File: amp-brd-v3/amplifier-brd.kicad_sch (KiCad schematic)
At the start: 12 parts, among them J1 VOUT, J2 VOUT, Q1 BSS84, U3 DS28EA00

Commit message: Modified DAC, AMP v2 and Mezzanine to support AMP v3. Finished AMP v3 design.
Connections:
- net EN: now also BOT1.38 (Pin_38), TOP1.38 (Pin_38)
- net GND: no longer BOT1.38 (Pin_38), TOP1.38 (Pin_38)
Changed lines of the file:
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@@
-	)
-	(junction
-		(at 250.19 83.82)
-		(diameter 0)
-		(color 0 0 0 0)
 	)
 	(junction
@@
 	(junction
 		(at 154.94 106.68)
-		(diameter 0)
-		(color 0 0 0 0)
-	)
-	(junction
-		(at 190.5 83.82)
 		(diameter 0)
 		(color 0 0 0 0)
@@
 	(wire
 		(pts
-			(xy 177.8 83.82) (xy 190.5 83.82)
-		)
-		(stroke
-			(width 0)
-			(type default)
-		)
-	)
-	(wire
-		(pts
 			(xy 154.94 121.92) (xy 165.1 121.92)
 		)
@@
 	(wire
 		(pts
-			(xy 190.5 83.82) (xy 190.5 99.06)
+			(xy 190.5 81.28) (xy 190.5 99.06)
 		)
 		(stroke
@@
 	(wire
 		(pts
-			(xy 250.19 81.28) (xy 250.19 83.82)
+			(xy 250.19 81.28) (xy 250.19 99.06)
 		)
 		(stroke
@@
 	(wire
 		(pts
+			(xy 177.8 83.82) (xy 186.69 83.82)
+		)
+		(stroke
+			(width 0)
+			(type default)
+		)
+	)
+	(wire
+		(pts
 			(xy 45.72 90.17) (xy 55.88 90.17)
 		)
@@
 	(wire
 		(pts
-			(xy 250.19 83.82) (xy 250.19 99.06)
-		)
-		(stroke
-			(width 0)
-			(type default)
-		)
-	)
-	(wire
-		(pts
 			(xy 214.63 111.76) (xy 224.79 111.76)
 		)
@@
 	(wire
 		(pts
-			(xy 190.5 81.28) (xy 190.5 83.82)
-		)
-		(stroke
-			(width 0)
-			(type default)
-		)
-	)
-	(wire
-		(pts
 			(xy 171.45 135.89) (xy 171.45 139.7)
 		)
@@
 	(wire
 		(pts
+			(xy 237.49 83.82) (xy 246.38 83.82)
+		)
+		(stroke
+			(width 0)
+			(type default)
+		)
+	)
+	(wire
+		(pts
 			(xy 214.63 104.14) (xy 214.63 106.68)
 		)
@@
 		(pts
 			(xy 177.8 114.3) (xy 186.69 114.3)
-		)
-		(stroke
-			(width 0)
-			(type default)
-		)
-	)
-	(wire
-		(pts
-			(xy 237.49 83.82) (xy 250.19 83.82)
 		)
 		(stroke
@@
 		)
 	)
+	(label "EN"
+		(at 246.38 83.82 180)
+		(effects
+			(font
+				(size 1.27 1.27)
+			)
+			(justify right bottom)
+		)
+	)
 	(label "A1"
 		(at 45.72 81.28 0)
@@
 		)
 	)
+	(label "EN"
+		(at 186.69 83.82 180)
+		(effects
+			(font
+				(size 1.27 1.27)
+			)
+			(justify right bottom)
+		)
+	)

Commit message: Optimized temperature sensor from Kuravi's design, reworked inductor placement in amp board v3
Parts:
- R7: value 10k -> 100k
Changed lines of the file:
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@@
 			)
 		)
-		(property "Value" "10k"
+		(property "Value" "100k"
 			(at 110.49 124.4599 0)
 			(effects

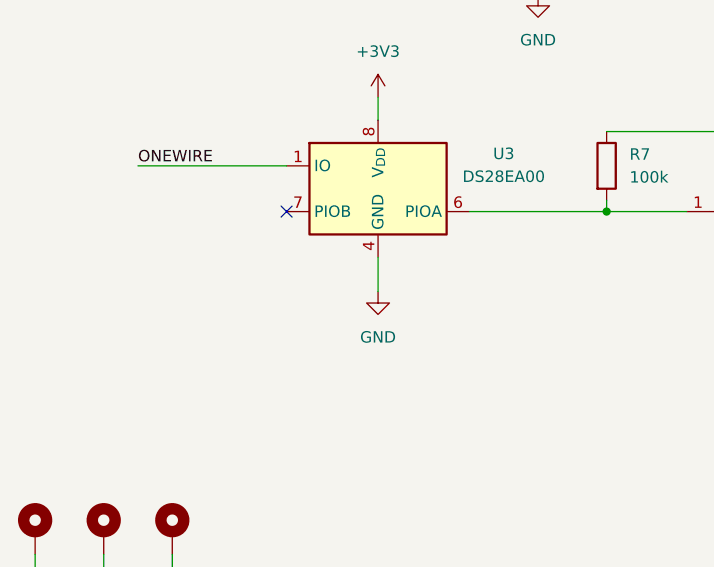
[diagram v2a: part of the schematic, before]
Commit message: Tested DAC and INA, doing new boards
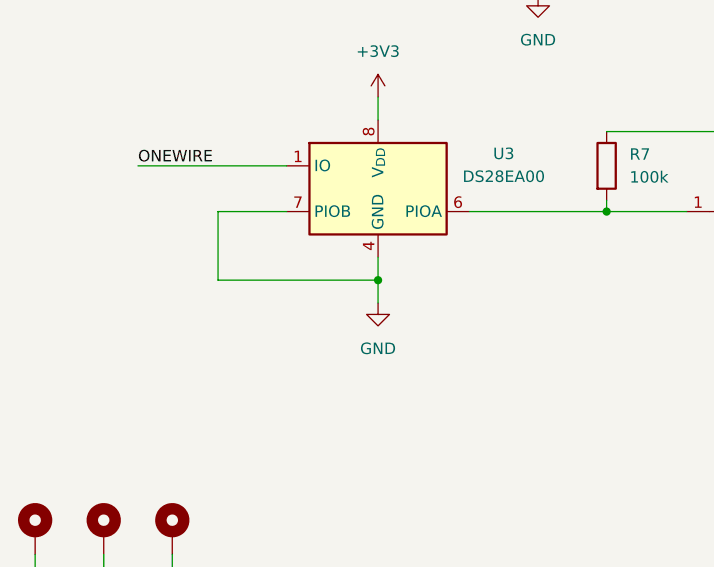
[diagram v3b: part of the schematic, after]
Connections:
- net GND: now also U3.7 (PIOB)
- no-connect marks 3 -> 2
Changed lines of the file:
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@@
+	)
+	(junction
+		(at 82.55 135.89)
+		(diameter 0)
+		(color 0 0 0 0)
 	)
 	(junction
@@
 	)
 	(no_connect
-		(at 72.39 128.27)
-	)
-	(no_connect
 		(at 186.69 96.52)
 	)
@@
 	(wire
 		(pts
+			(xy 82.55 135.89) (xy 82.55 138.43)
+		)
+		(stroke
+			(width 0)
+			(type default)
+		)
+	)
+	(wire
+		(pts
 			(xy 154.94 88.9) (xy 165.1 88.9)
 		)
@@
 	(wire
 		(pts
+			(xy 72.39 128.27) (xy 64.77 128.27)
+		)
+		(stroke
+			(width 0)
+			(type default)
+		)
+	)
+	(wire
+		(pts
 			(xy 59.69 168.91) (xy 59.69 166.37)
 		)
@@
 	(wire
 		(pts
-			(xy 82.55 133.35) (xy 82.55 137.16)
+			(xy 82.55 133.35) (xy 82.55 135.89)
 		)
 		(stroke
@@
 	(wire
 		(pts
+			(xy 64.77 128.27) (xy 64.77 135.89)
+		)
+		(stroke
+			(width 0)
+			(type default)
+		)
+	)
+	(wire
+		(pts
 			(xy 44.45 166.37) (xy 44.45 168.91)
 		)
@@
 		(pts
 			(xy 214.63 91.44) (xy 224.79 91.44)
+		)
+		(stroke
+			(width 0)
+			(type default)
+		)
+	)
+	(wire
+		(pts
+			(xy 64.77 135.89) (xy 82.55 135.89)
 		)
 		(stroke
@@
 	(symbol
 		(lib_id "power:GND")
-		(at 82.55 137.16 0)
+		(at 82.55 138.43 0)
 		(unit 1)
 		(exclude_from_sim no)
@@
 		(fields_autoplaced yes)
 		(property "Reference" "#PWR021"
+			(at 82.55 144.78 0)
+			(effects
+				(font
+					(size 1.27 1.27)
+				)
+				(hide yes)
+			)
+		)
+		(property "Value" "GND"
 			(at 82.55 143.51 0)
 			(effects
@@
 					(size 1.27 1.27)
 				)
-				(hide yes)
-			)
-		)
-		(property "Value" "GND"
-			(at 82.55 142.24 0)
-			(effects
-				(font
-					(size 1.27 1.27)
-				)
 			)
 		)
 		(property "Footprint" ""
-			(at 82.55 137.16 0)
+			(at 82.55 138.43 0)
 			(effects
 				(font
@@
 		)
 		(property "Datasheet" ""
-			(at 82.55 137.16 0)
+			(at 82.55 138.43 0)
 			(effects
 				(font
@@
 		)
 		(property "Description" "Power symbol creates a global label with name \"GND\" , ground"
-			(at 82.55 137.16 0)
-			(effects
-				(font
+			(at 82.55 138.43 0)
+			(effects
+				(font

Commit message: Updated all boards for production
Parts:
- removed J2: VOUT, Connector_PinHeader_2.54mm:PinHeader_1x02_P2.54mm_Vertical, symbol Connector_Generic:Conn_01x02
- J1: footprint Connector_Molex:Molex_PicoBlade_53261-0471_1x04-1MP_P1.25mm_Horizontal -> Connector_Molex:Molex_PicoBlade_53261-0271_1x02-1MP_P1.25mm_Horizontal; symbol Connector_Generic_MountingPin:Conn_01x04_MountingPin -> Connector_Generic_MountingPin:Conn_01x02_MountingPin; Mfr # 53261-0471 -> 53261-0271; Mouser https://www.mouser.com/ProductDetail/Molex/53261-0471?qs=%2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 -> https://www.mouser.com/ProductDetail/Molex/53261-0271?qs=%2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; Mouser # 538-53261-0471 -> 538-53261-0271
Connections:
- net GND: now also J1.2 (Pin_2); no longer J1.3 (Pin_3), J1.4 (Pin_4)
- net OP AMP/V_{OUT}: no longer J1.2 (Pin_2)
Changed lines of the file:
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@@
-	)
-	(junction
-		(at 110.49 96.52)
-		(diameter 0)
-		(color 0 0 0 0)
 	)
 	(junction
@@
 	)
 	(junction
-		(at 102.87 81.28)
-		(diameter 0)
-		(color 0 0 0 0)
-	)
-	(junction
 		(at 214.63 106.68)
 		(diameter 0)
@@
 	)
 	(junction
-		(at 102.87 86.36)
-		(diameter 0)
-		(color 0 0 0 0)
-	)
-	(junction
 		(at 214.63 116.84)
 		(diameter 0)
@@
 	(junction
 		(at 154.94 106.68)
-		(diameter 0)
-		(color 0 0 0 0)
-	)
-	(junction
-		(at 102.87 83.82)
 		(diameter 0)
 		(color 0 0 0 0)
@@
 	(wire
 		(pts
-			(xy 86.36 83.82) (xy 102.87 83.82)
+			(xy 86.36 83.82) (xy 105.41 83.82)
 		)
 		(stroke
@@
 	(wire
 		(pts
-			(xy 119.38 78.74) (xy 102.87 78.74)
-		)
-		(stroke
-			(width 0)
-			(type default)
-		)
-	)
-	(wire
-		(pts
 			(xy 154.94 99.06) (xy 165.1 99.06)
 		)
@@
 	(wire
 		(pts
-			(xy 102.87 88.9) (xy 102.87 86.36)
-		)
-		(stroke
-			(width 0)
-			(type default)
-		)
-	)
-	(wire
-		(pts
 			(xy 151.13 124.46) (xy 151.13 127)
 		)
@@
 	(wire
 		(pts
-			(xy 105.41 81.28) (xy 102.87 81.28)
-		)
-		(stroke
-			(width 0)
-			(type default)
-		)
-	)
-	(wire
-		(pts
 			(xy 231.14 135.89) (xy 231.14 139.7)
 		)
@@
 	(wire
 		(pts
-			(xy 102.87 86.36) (xy 100.33 86.36)
-		)
-		(stroke
-			(width 0)
-			(type default)
-		)
-	)
-	(wire
-		(pts
-			(xy 119.38 86.36) (xy 119.38 96.52)
+			(xy 100.33 86.36) (xy 105.41 86.36)
 		)
 		(stroke
@@
 	(wire
 		(pts
-			(xy 110.49 93.98) (xy 110.49 96.52)
-		)
-		(stroke
-			(width 0)
-			(type default)
-		)
-	)
-	(wire
-		(pts
-			(xy 121.92 86.36) (xy 119.38 86.36)
-		)
-		(stroke
-			(width 0)
-			(type default)
-		)
-	)
-	(wire
-		(pts
 			(xy 214.63 99.06) (xy 214.63 101.6)
 		)
@@
 	(wire
 		(pts
-			(xy 110.49 96.52) (xy 119.38 96.52)
-		)
-		(stroke
-			(width 0)
-			(type default)
-		)
-	)
-	(wire
-		(pts
 			(xy 237.49 93.98) (xy 246.38 93.98)
 		)
@@
 	(wire
 		(pts
-			(xy 121.92 83.82) (xy 119.38 83.82)
-		)
-		(stroke
-			(width 0)
-			(type default)
-		)
-	)
-	(wire
-		(pts
 			(xy 55.88 123.19) (xy 72.39 123.19)
 		)
@@
 	(wire
 		(pts
-			(xy 102.87 81.28) (xy 102.87 83.82)
-		)
-		(stroke
-			(width 0)
-			(type default)
-		)
-	)
-	(wire
-		(pts
 			(xy 250.19 135.89) (xy 231.14 135.89)
 		)
@@
 	(wire
 		(pts
-			(xy 119.38 83.82) (xy 119.38 78.74)
-		)
-		(stroke
-			(width 0)
-			(type default)
-		)
-	)
-	(wire
-		(pts
 			(xy 237.49 78.74) (xy 250.19 78.74)
 		)
@@
 	(wire
 		(pts
-			(xy 105.41 88.9) (xy 102.87 88.9)
-		)
-		(stroke
-			(width 0)
-			(type default)
-		)
-	)
-	(wire
-		(pts
 			(xy 100.33 86.36) (xy 100.33 96.52)
 		)
@@
 	(wire
 		(pts
-			(xy 102.87 78.74) (xy 102.87 81.28)
+			(xy 110.49 91.44) (xy 110.49 96.52)
 		)
 		(stroke
@@
 		(pts
 			(xy 52.07 166.37) (xy 52.07 168.91)
-		)
-		(stroke
-			(width 0)
-			(type default)
-		)
-	)
-	(wire
-		(pts
-			(xy 102.87 83.82) (xy 105.41 83.82)
-		)
-		(stroke
-			(width 0)
-			(type default)
-		)
-	)
-	(wire
-		(pts
-			(xy 105.41 86.36) (xy 102.87 86.36)
 		)
 		(stroke
@@
 			)
 			(justify right bottom)
-		)
-	)
-	(symbol
-		(lib_id "Connector_Generic:Conn_01x02")
-		(at 127 83.82 0)
-		(unit 1)
-		(exclude_from_sim no)
-		(in_bom yes)
-		(on_board yes)
-		(dnp yes)
-		(fields_autoplaced yes)
-		(property "Reference" "J2"
-			(at 129.54 83.8199 0)
-			(effects
-				(font
-					(size 1.27 1.27)
-				)
-				(justify left)
-			)
-		)
-		(property "Value" "VOUT"
-			(at 129.54 86.3599 0)
-			(effects
-				(font
-					(size 1.27 1.27)
-				)
-				(justify left)
-			)
-		)
-		(property "Footprint" "Connector_PinHeader_2.54mm:PinHeader_1x02_P2.54mm_Vertical"
-			(at 127 83.82 0)
-			(effects
-				(font
-					(size 1.27 1.27)
-				)
-				(hide yes)
-			)
-		)
-		(property "Datasheet" "~"
-			(at 127 83.82 0)
-			(effects
-				(font
-					(size 1.27 1.27)
-				)
-				(hide yes)
-			)
-		)
-		(property "Description" "Generic connector, single row, 01x02, script generated (kicad-library-utils/schlib/autogen/connector/)"
-			(at 127 83.82 0)
-			(effects
-				(font
-					(size 1.27 1.27)
-				)
-				(hide yes)
-			)
-		)
-		(pin "2"
-		)
-		(pin "1"
-		)
-		(instances
-			(project ""
-				(path "/4a199ccc-be1f-4132-9551-a46e36599bcb"
-					(reference "J2")
-					(unit 1)
-				)
-			)
 		)
 	)
@@
 	)
 	(symbol
-		(lib_id "Connector_Generic_MountingPin:Conn_01x04_MountingPin")
+		(lib_id "Connector_Generic_MountingPin:Conn_01x02_MountingPin")
 		(at 110.49 83.82 0)
 		(unit 1)
@@
 			)
 		)
-		(property "Footprint" "Connector_Molex:Molex_PicoBlade_53261-0471_1x04-1MP_P1.25mm_Horizontal"
+		(property "Footprint" "Connector_Molex:Molex_PicoBlade_53261-0271_1x02-1MP_P1.25mm_Horizontal"
 			(at 110.49 83.82 0)
 			(effects
@@
 			)
 		)
-		(property "Datasheet" "https://www.molex.com/en-us/products/part-detail-pdf/532610471?display=pdf"
+		(property "Datasheet" "~"
 			(at 110.49 83.82 0)
 			(effects
@@
 			)
 		)
-		(property "Description" "Headers & Wire Housings PicoBlade1.25 SMT RA PKG 4P"
+		(property "Description" "Headers & Wire Housings PicoBlade1.25 SMT RA PKG 2P"
 			(at 110.49 83.82 0)
 			(effects
@@
 			)
 		)
-		(property "Mfr #" "53261-0471"
+		(property "Mfr #" "53261-0271"
 			(at 110.49 83.82 0)
 			(effects
@@
 			)
 		)
-		(property "Mouser #" "538-53261-0471"
+		(property "Mouser #" "538-53261-0271"
 			(at 110.49 83.82 0)
 			(effects
@@
 			)
 		)
-		(property "Mouser" "https://www.mouser.com/ProductDetail/Molex/53261-0471?qs=%252B72YyncTwW9e3et3PwnEMw%3D%3D&utm_id=22310811105&utm_source=google&utm_medium=cpc&utm_marketing_tactic=amermsp&gad_source=1&gad_campaignid=22310815365&gbraid=0AAAAADn_wf1zNbovdi8o5BkocC-mYGcy3&gclid=Cj0KCQiAosrJBhD0ARIsAHebCNoqHSlv8093uII-LEywz99gd4VTBqkxKpseFi77wLe4p3ZZiX-RvZsaAr9zEALw_wcB"
+		(property "Mouser" "https://www.mouser.com/ProductDetail/Molex/53261-0271?qs=%252B72YyncTwW%252B8%252BBjraxGf3A%3D%3D"
 			(at 110.49 83.82 0)
 			(effects
@@
 		(pin "1"
 		)
-		(pin "3"
-		)
-		(pin "4"
-		)
 		(pin "2"

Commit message: Added part numbers
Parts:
- BOT1: Mfr (none) -> Amphenol FCI; Mfr # (none) -> 10132798-042100LF; Package (none) -> SMD
- D1: Mfr (none) -> Dialight; Mfr # (none) -> 598-2A00-107F; Package (none) -> 0402
- J1: Package (none) -> SMD
- Q1: Mfr (none) -> onsemi; Mfr # (none) -> BSS84; Package (none) -> SOT-23
- R6: Mfr (none) -> TE Connectivity / Holsworthy; Mfr # (none) -> RP73PF1E1K0BTD; Package (none) -> 0402
- R7: Mfr (none) -> Vishay-Dale; Mfr # (none) -> CRCW0402100KFKED; Package (none) -> 0402
- TOP1: Mfr (none) -> Amphenol ICC (FCI); Mfr # (none) -> 10132797-045100LF; Package (none) -> SMD
- U3: Mfr (none) -> Analog Devices Inc./Maxim Integrated; Mfr # (none) -> DS28EA00U+; Package (none) -> SMD
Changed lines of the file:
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@@
+			)
+		)
+		(property "Package" "SMD"
+			(at 110.49 83.82 0)
+			(effects
+				(font
+					(size 1.27 1.27)
+				)
+				(hide yes)
 			)
 		)
@@
 			)
 		)
-		(property "Description" "Generic connectable mounting pin connector, double row, 02x20, counter clockwise pin numbering scheme (similar to DIP package numbering), script generated (kicad-library-utils/schlib/autogen/connector/)"
+		(property "Description" "Board to Board & Mezzanine Connectors HEIGHT REC CONNECTOR"
+			(at 229.87 101.6 0)
+			(effects
+				(font
+					(size 1.27 1.27)
+				)
+				(hide yes)
+			)
+		)
+		(property "Package" "SMD"
+			(at 229.87 101.6 0)
+			(effects
+				(font
+					(size 1.27 1.27)
+				)
+				(hide yes)
+			)
+		)
+		(property "Mfr" "Amphenol FCI"
+			(at 229.87 101.6 0)
+			(effects
+				(font
+					(size 1.27 1.27)
+				)
+				(hide yes)
+			)
+		)
+		(property "Mfr #" "10132798-042100LF"
 			(at 229.87 101.6 0)
 			(effects
@@
 			)
 		)
-		(property "Description" "Light emitting diode"
+		(property "Description" "White LEDs 0402 SMD WHITE 5mA 2.4V 66mW"
 			(at 124.46 156.21 0)
 			(effects
@@
 			)
 		)
+		(property "Package" "0402"
+			(at 124.46 156.21 90)
+			(effects
+				(font
+					(size 1.27 1.27)
+				)
+				(hide yes)
+			)
+		)
+		(property "Mfr #" "598-2A00-107F "
+			(at 124.46 156.21 90)
+			(effects
+				(font
+					(size 1.27 1.27)
+				)
+				(hide yes)
+			)
+		)
+		(property "Mfr" "Dialight "
+			(at 124.46 156.21 90)
+			(effects
+				(font
+					(size 1.27 1.27)
+				)
+				(hide yes)
+			)
+		)
 		(pin "2"
 		)
@@
 			)
 		)
-		(property "Description" "1-Wire Digital Thermometer with Sequence Detect and PIO"
+		(property "Description" "Temperature Sensor Digital, Local -40°C ~ 85°C 11 b 8-uMAX/uSOP"
+			(at 82.55 125.73 0)
+			(effects
+				(font
+					(size 1.27 1.27)
+				)
+				(hide yes)
+			)
+		)
+		(property "Mfr" "Analog Devices Inc./Maxim Integrated"
+			(at 82.55 125.73 0)
+			(effects
+				(font
+					(size 1.27 1.27)
+				)
+				(hide yes)
+			)
+		)
+		(property "Mfr #" "DS28EA00U+"
+			(at 82.55 125.73 0)
+			(effects
+				(font
+					(size 1.27 1.27)
+				)
+				(hide yes)
+			)
+		)
+		(property "Package" "SMD"
 			(at 82.55 125.73 0)
 			(effects
@@
 			)
 		)
-		(property "Description" "Generic connectable mounting pin connector, double row, 02x20, counter clockwise pin numbering scheme (similar to DIP package numbering), script generated (kicad-library-utils/schlib/autogen/connector/)"
+		(property "Description" "40 Position Connector Plug, Outer Shroud Contacts Surface Mount Gold"
+			(at 170.18 101.6 0)
+			(effects
+				(font
+					(size 1.27 1.27)
+				)
+				(hide yes)
+			)
+		)
+		(property "Mfr" "Amphenol ICC (FCI)"
+			(at 170.18 101.6 0)
+			(effects
+				(font
+					(size 1.27 1.27)
+				)
+				(hide yes)
+			)
+		)
+		(property "Mfr #" "10132797-045100LF"
+			(at 170.18 101.6 0)
+			(effects
+				(font
+					(size 1.27 1.27)
+				)
+				(hide yes)
+			)
+		)
+		(property "Package" "SMD"
 			(at 170.18 101.6 0)
 			(effects
@@
 			)
 		)
-		(property "Description" "Resistor"
+		(property "Description" "Thin Film Resistors HP PrecisionResistor 1E 0.1W 1K0"
+			(at 124.46 143.51 0)
+			(effects
+				(font
+					(size 1.27 1.27)
+				)
+				(hide yes)
+			)
+		)
+		(property "Package" "0402"
+			(at 124.46 143.51 0)
+			(effects
+				(font
+					(size 1.27 1.27)
+				)
+				(hide yes)
+			)
+		)
+		(property "Mfr" "TE Connectivity / Holsworthy "
+			(at 124.46 143.51 0)
+			(effects
+				(font
+					(size 1.27 1.27)
+				)
+				(hide yes)
+			)
+		)
+		(property "Mfr #" "RP73PF1E1K0BTD "
 			(at 124.46 143.51 0)
 			(effects
@@
 			)
 		)
-		(property "Description" "Resistor"
+		(property "Description" "Thick Film Resistors - SMD 1/10 Watt 100Kohms 1%"
+			(at 107.95 123.19 0)
+			(effects
+				(font
+					(size 1.27 1.27)
+				)
+				(hide yes)
+			)
+		)
+		(property "Mfr" "Vishay-Dale"
+			(at 107.95 123.19 0)
+			(effects
+				(font
+					(size 1.27 1.27)
+				)
+				(hide yes)
+			)
+		)
+		(property "Mfr #" "CRCW0402100KFKED"
+			(at 107.95 123.19 0)
+			(effects
+				(font
+					(size 1.27 1.27)
+				)
+				(hide yes)
+			)
+		)
+		(property "Package" "0402"
 			(at 107.95 123.19 0)
 			(effects
@@
 			(at 121.92 128.27 0)
 			(effects
+				(font
+					(size 1.27 1.27)
+				)
+				(hide yes)
+			)
+		)
+		(property "Mfr" "onsemi"
+			(at 121.92 128.27 0)
+			(effects
+				(font
+					(size 1.27 1.27)
+				)
+				(hide yes)
+			)
+		)
+		(property "Mfr #" "BSS84"
+			(at 121.92 128.27 0)
+			(effects
+				(font
+					(size 1.27 1.27)
+				)
+				(hide yes)
+			)
+		)
+		(property "Package" "SOT-23"
+			(at 121.92 128.27 0)
+			(effects
